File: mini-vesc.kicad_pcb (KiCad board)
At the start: 4 copper layers, 65 x 18 mm, 151 parts, among them P1 CONN_1, P10 CONN_01X06, P11 CONN_01X06, P2 CONN_1, P3 CONN_1, P4 CONN_1, P5 CONN_1, P6 CONN_1, P9 CONN_01X06, Q1 NTMFS5C604NLT1G, Q2 NTMFS5C604NLT1G, Q3 NTMFS5C604NLT1G, Q4 NTMFS5C604NLT1G, Q5 NTMFS5C604NLT1G, Q6 NTMFS5C604NLT1G, U1 LM5113, U10 MCP1700, U2 LM5113, U3 LM5113, U4 AD8418, U5 AD8418, U6 AD8418, U7 STM32F40X_LQFP64, U8 LMR16006, U9 MCP1700, X1 ABM3B-8.000MHZ

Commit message: Playing around with routing
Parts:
- removed C1, C2, C3: 470n, Capacitor_SMD:C_0603_1608Metric
- removed C10, C11, C17, C18, C6, C7, C77, C78, C8, C86, C87, C88, C89, C9, C90: 2u2, Capacitor_SMD:C_0603_1608Metric
- removed C12, C13, C25, C28, C32, C39, C4, C48, C5, C60, C61, C62, C63, C74, C75, C84, C85: 10u, Capacitor_SMD:C_1206_3216Metric
- removed C14, C15, C16: 4n7, Capacitor_SMD:C_0603_1608Metric
- removed C19, C20, C21, C22, C26, C27, C29, C76: 100n, Capacitor_SMD:C_0603_1608Metric
- removed C23: 220nF, Capacitor_SMD:C_0603_1608Metric
- removed C24: 2u2, Capacitor_SMD:C_1206_3216Metric
- removed C30, C31: 10pF, Capacitor_SMD:C_0603_1608Metric
- removed C33, C34, C35, C36, C37, C38, C40, C41, C42, C43, C44, C45, C46, C47, C49, C50, C51, C52, C53, C54, C55, C56, C57, C58, C59, C64, C65, C66, C67, C68, C69, C70, C71, C72, C73, C83: C, Capacitor_SMD:C_1206_3216Metric
- removed D1: D_Schottky, Diode_SMD:D_SOD-123
- removed D3, D4: LED, LED_SMD:LED_0603_1608Metric
- removed L1: Wurth Electronics 74438335220, mojaKniznica:WE-MAPI
- removed P1, P2, P3, P4, P5, P6: CONN_1, kicad_subory:prekov
- removed P10, P11, P9: CONN_01X06, kicad_subory:JST_ZH_1.5_6-Pin
- removed Q1, Q2, Q5, Q6: NTMFS5C604NLT1G, kicad_subory:DFN5
- removed R1, R2, R3: R0005, mojaKniznica:2512Rv2
- removed R10, R11, R6, R7, R8, R9: 3R9, Resistor_SMD:R_0603_1608Metric
- removed R12, R14, R4: 39k, Resistor_SMD:R_0603_1608Metric
- removed R13, R15, R17, R5: 2k2, Resistor_SMD:R_0603_1608Metric
- removed R16: 25k5, Resistor_SMD:R_0603_1608Metric
- removed R18, R19, R20, R30: 100R, Resistor_SMD:R_0603_1608Metric
- removed R21, R31, R34: 10k, Resistor_SMD:R_0603_1608Metric
- removed R28, R29: 220R, Resistor_SMD:R_0603_1608Metric
- removed R32: 10kNTC, Resistor_SMD:R_0603_1608Metric
- removed R33: 100k, Resistor_SMD:R_0603_1608Metric
- removed U1, U2, U3: LM5113, kicad_subory:WSON10_
- removed U10, U9: MCP1700, TO_SOT_Packages_SMD:SOT-23
- removed U4: AD8418, Package_SO:MSOP-8_3x3mm_P0.65mm
- removed U7: STM32F40X_LQFP64, Package_QFP:LQFP-64_10x10mm_P0.5mm
- removed U8: LMR16006, Package_TO_SOT_SMD:SOT-23-6
- removed X1: ABM3B-8.000MHZ, mojaKniznica:5x3.2KRISTALL
- added R23: 3.9Ω, Resistor_SMD:R_0402_1005Metric, F.Cu at (123.0, 68.8)
- added R24: 39kΩ, Resistor_SMD:R_0402_1005Metric, B.Cu at (119.7, 67.3)
- added R26: 500µΩ, Footprints:R_Shunt_Bourns_CSS2H-2512_6332Metric, B.Cu at (124.4, 64.0)
- C79: value 10u -> 2.2µF; footprint Capacitor_SMD:C_1206_3216Metric -> Capacitor_SMD:C_0402_1005Metric; moved to F.Cu
- C80: value 10u -> 470nF; footprint Capacitor_SMD:C_1206_3216Metric -> Capacitor_SMD:C_0402_1005Metric
- C81: value C -> 2.2µF; footprint Capacitor_SMD:C_1206_3216Metric -> Capacitor_SMD:C_0402_1005Metric
- C82: value 10u -> 4.7nF; footprint Capacitor_SMD:C_1206_3216Metric -> Capacitor_SMD:C_0402_1005Metric
- Q3: footprint kicad_subory:DFN5 -> Package_SO:ONSemi_SO-8FL_488AA; moved to F.Cu
- Q4: footprint kicad_subory:DFN5 -> Package_SO:ONSemi_SO-8FL_488AA
- R22: value 54k9 -> 3.9Ω; footprint Resistor_SMD:R_0603_1608Metric -> Resistor_SMD:R_0402_1005Metric
- R25: value 22R -> 2.2kΩ; footprint Resistor_SMD:R_0603_1608Metric -> Resistor_SMD:R_0402_1005Metric
- R27: value 22R -> 100Ω; footprint Resistor_SMD:R_0603_1608Metric -> Resistor_SMD:R_0402_1005Metric
- U5: value AD8418 -> LM5113-Q1; footprint Package_SO:MSOP-8_3x3mm_P0.65mm -> Footprints:WSON-10-1EP_4x4mm_P0.8mm_EP2.6x3mm_ThermalVias
- U6: value AD8418 -> AD8417; moved to B.Cu
- moved U5 52.8 mm to (119.9, 70.0)
- moved U6 52.7 mm to (124.4, 67.8), turned to 180 degrees
- moved Q4 48.8 mm to (121.4, 64.0)
- moved Q3 43.9 mm to (114.4, 64.0), turned to 180 degrees
- moved C81 30.1 mm to (120.7, 67.3), turned to -90 degrees
- moved C82 30.0 mm to (123.3, 70.5), turned to -90 degrees
- moved R25 29.4 mm to (118.7, 67.3), turned to -90 degrees
- moved R27 22.4 mm to (122.3, 70.5)
- moved C79 20.3 mm to (118.4, 67.3), turned to 0 degrees
- moved C80 18.7 mm to (117.3, 70.4), turned to -90 degrees
- moved R22 14.6 mm to (116.7, 70.4), turned to 90 degrees
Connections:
- C79 pad 1: VDD -> +5V
- C80 pad 1: VDD -> Net-(U5-HB)
- C80 pad 2: VSS -> /Half Bridge W/Output
- C81 pad 1: VDD -> VSS
- C81 pad 2: VSS -> VAA
- C82 pad 1: VDD -> VSS
- C82 pad 2: VSS -> I_{senseW}
- Q3 pad 1: Net-(Q3-G) -> /Half Bridge W/Output
- Q3 pad 2: SH2 -> /Half Bridge W/Output
- Q3 pad 3: VDD -> /Half Bridge W/Output
- Q4 pad 1: Net-(Q4-G) -> VSS
- Q4 pad 3: SH2 -> VSS
- R22 pad 1: +5V -> /Half Bridge W/HighGate
- R22 pad 2: Net-(U8-FB) -> Net-(U5-HOH)
- R25 pad 1: Net-(P10-Pin_4) -> VSS
- R25 pad 2: USB-DM -> V_{senseW}
- R27 pad 1: Net-(P10-Pin_5) -> Net-(U6-OUT)
- R27 pad 2: USB-DP -> I_{senseW}
- U5 pad 1: Net-(P2-Pad1) -> +5V
- U5 pad 2: VSS -> Net-(U5-HB)
- U5 pad 3: VSS -> Net-(U5-HOH)
- U5 pad 4: Net-(U5-Pad4) -> /Half Bridge W/HighGate
- U5 pad 5: I2 -> /Half Bridge W/Output
- U5 pad 6: VAA -> HI3
- U5 pad 7: VAA -> LI3
- U5 pad 8: SH2 -> VSS
- U6 pad 1: Net-(P3-Pad1) -> /W
- U6 pad 4: Net-(U6-Pad4) -> unconnected-(U6-NC-Pad4)
- U6 pad 5: I3 -> Net-(U6-OUT)
- U6 pad 8: SH3 -> /Half Bridge W/Output
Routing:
- net VSS: track 298.6 -> 8.32 mm, vias 57 -> 0
- net +5V: track 162.2 -> 1.11 mm, vias 6 -> 0
- net VAA: track 134.2 -> 3.44 mm, vias 6 -> 0
- net VDD: track 93.0 -> 0.00 mm, vias 30 -> 0
- net VCC: track 82.9 -> 0.00 mm, vias 6 -> 0
- net Net-(C77-Pad2): track 67.6 -> 0.00 mm
- net I1: track 60.9 -> 0.00 mm, vias 2 -> 0
- net I3: track 60.2 -> 0.00 mm, vias 2 -> 0
- net SENS_3: track 53.9 -> 0.00 mm, vias 2 -> 0
- net SENS_2: track 51.4 -> 0.00 mm, vias 2 -> 0
- net SENS_1: track 49.8 -> 0.00 mm, vias 2 -> 0
- net I2: track 48.2 -> 0.00 mm, vias 2 -> 0
- net ADC_EXT1: track 41.7 -> 0.00 mm, vias 3 -> 0
- net HI2: track 31.2 -> 0.00 mm, vias 2 -> 0
- net TX: track 29.4 -> 0.00 mm, vias 1 -> 0
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- added copper zone on B.Cu, net /Half Bridge W/Output
- added copper zone on F.Cu, net /Half Bridge W/Output
- removed copper zone on F.Cu, net +5V
- removed copper zone on F.Cu, net Net-(D1-K)
- removed copper zone on B.Cu, net Net-(U4-IN-)
- removed copper zone on F.Cu, net Net-(U4-IN-)
- removed copper zone on In1.Cu, net Net-(U4-IN-)
- removed copper zone on In2.Cu, net Net-(U4-IN-)
- removed copper zone on B.Cu, net Net-(U5-IN-)
- removed copper zone on F.Cu, net Net-(U5-IN-)
- removed copper zone on In1.Cu, net Net-(U5-IN-)
- removed copper zone on In2.Cu, net Net-(U5-IN-)
- removed copper zone on B.Cu, net Net-(U6-IN-)
- removed copper zone on F.Cu, net Net-(U6-IN-)
- removed copper zone on In1.Cu, net Net-(U6-IN-)
- removed copper zone on In2.Cu, net Net-(U6-IN-)
- removed copper zone on B.Cu, net SH1
- removed copper zone on F.Cu, net SH1
- removed copper zone on B.Cu, net SH2
- removed copper zone on F.Cu, net SH2
- removed copper zone on B.Cu, net SH3
- removed copper zone on F.Cu, net SH3
- removed copper zone on B.Cu, net VDD
- removed copper zone on F.Cu, net VDD
- removed copper zone on In1.Cu, net VDD
- removed copper zone on In2.Cu, net VDD
- removed copper zone on B.Cu, net VSS
- removed copper zone on F.Cu, net VSS
- removed copper zone on In1.Cu, net VSS
- removed copper zone on In2.Cu, net VSS
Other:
- board size 65 x 18 mm -> 65 x 40 mm
- board text removed: "+5V"
- board text removed: "A1"
- board text removed: "A2"
- board text removed: "DM"
- board text removed: "DP"
- board text removed: "GND"
- board text removed: "H1"
- board text removed: "H2"
- board text removed: "H3"
- board text removed: "PPM"
- board text removed: "RX"
- board text removed: "SWC"
- board text removed: "SWD"
- board text removed: "T"
- board text removed: "TX"

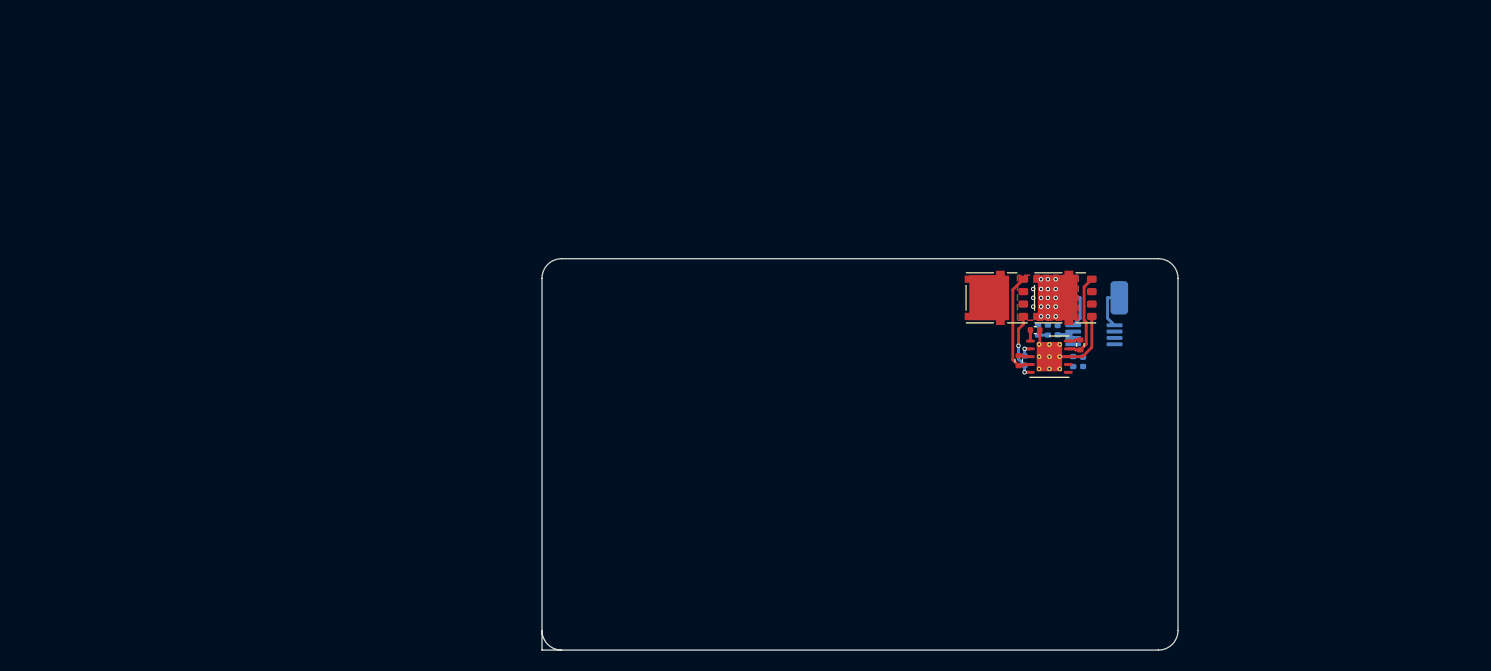
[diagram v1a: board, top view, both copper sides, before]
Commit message: Playing with routing some more, trying to determine board size
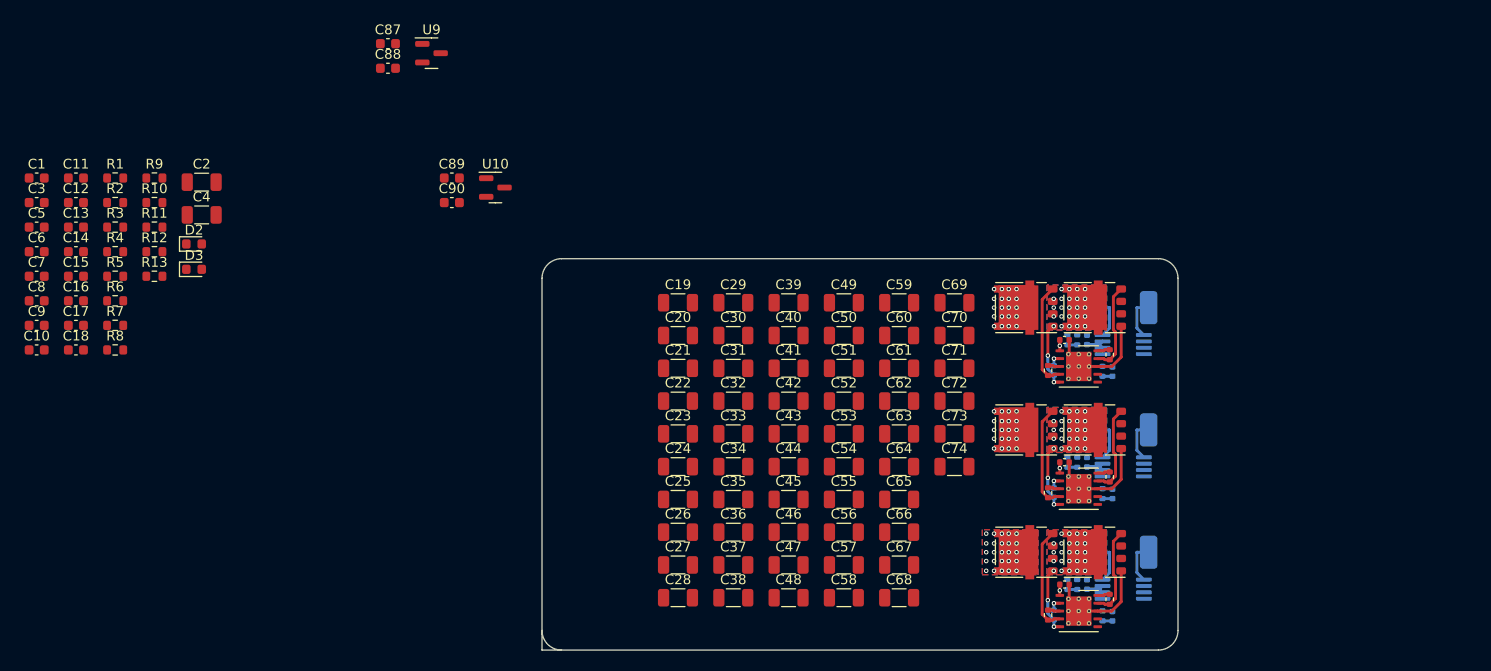
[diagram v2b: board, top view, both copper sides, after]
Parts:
- added C1: 220nF, Capacitor_SMD:C_0603_1608Metric, F.Cu at (16.4, 51.8)
- added C10: 2.2µF, Capacitor_SMD:C_0603_1608Metric, F.Cu at (16.4, 69.3)
- added C11: 2.2µF, Capacitor_SMD:C_0603_1608Metric, F.Cu at (20.4, 51.8)
- added C12: 10pF, Capacitor_SMD:C_0603_1608Metric, F.Cu at (20.4, 54.3)
- added C13: 2.2µF, Capacitor_SMD:C_0603_1608Metric, F.Cu at (20.4, 56.8)
- added C14: 2.2µF, Capacitor_SMD:C_0603_1608Metric, F.Cu at (20.4, 59.3)
- added C15: 100n, Capacitor_SMD:C_0603_1608Metric, F.Cu at (20.4, 61.8)
- added C16: 100nF, Capacitor_SMD:C_0603_1608Metric, F.Cu at (20.4, 64.3)
- added C17: 10pF, Capacitor_SMD:C_0603_1608Metric, F.Cu at (20.4, 66.8)
- added C18: 2.2µF, Capacitor_SMD:C_0603_1608Metric, F.Cu at (20.4, 69.3)
- added C19: 10u, Capacitor_SMD:C_1206_3216Metric, F.Cu at (81.9, 64.5)
- added C2: 2.2µF, Capacitor_SMD:C_1206_3216Metric, F.Cu at (33.2, 52.2)
- added C20: C, Capacitor_SMD:C_1206_3216Metric, F.Cu at (81.9, 67.8)
- added C21: C, Capacitor_SMD:C_1206_3216Metric, F.Cu at (81.9, 71.2)
- added C22: 10u, Capacitor_SMD:C_1206_3216Metric, F.Cu at (81.9, 74.5)
- added C23: C, Capacitor_SMD:C_1206_3216Metric, F.Cu at (81.9, 77.9)
- added C24: 10u, Capacitor_SMD:C_1206_3216Metric, F.Cu at (81.9, 81.2)
- added C25: C, Capacitor_SMD:C_1206_3216Metric, F.Cu at (81.9, 84.6)
- added C26: C, Capacitor_SMD:C_1206_3216Metric, F.Cu at (81.9, 88.0)
- added C27: C, Capacitor_SMD:C_1206_3216Metric, F.Cu at (81.9, 91.3)
- added C28: C, Capacitor_SMD:C_1206_3216Metric, F.Cu at (81.9, 94.7)
- added C29: 10u, Capacitor_SMD:C_1206_3216Metric, F.Cu at (87.5, 64.5)
- added C3: 100nF, Capacitor_SMD:C_0603_1608Metric, F.Cu at (16.4, 54.3)
- added C30: C, Capacitor_SMD:C_1206_3216Metric, F.Cu at (87.5, 67.8)
- added C31: 10u, Capacitor_SMD:C_1206_3216Metric, F.Cu at (87.5, 71.2)
- added C32: 10u, Capacitor_SMD:C_1206_3216Metric, F.Cu at (87.5, 74.5)
- added C33: C, Capacitor_SMD:C_1206_3216Metric, F.Cu at (87.5, 77.9)
- added C34: C, Capacitor_SMD:C_1206_3216Metric, F.Cu at (87.5, 81.2)
- added C35: C, Capacitor_SMD:C_1206_3216Metric, F.Cu at (87.5, 84.6)
- added C36: 10u, Capacitor_SMD:C_1206_3216Metric, F.Cu at (87.5, 88.0)
- added C37: C, Capacitor_SMD:C_1206_3216Metric, F.Cu at (87.5, 91.3)
- added C38: C, Capacitor_SMD:C_1206_3216Metric, F.Cu at (87.5, 94.7)
- added C39: 10u, Capacitor_SMD:C_1206_3216Metric, F.Cu at (93.2, 64.5)
- added C4: 10µF, Capacitor_SMD:C_1206_3216Metric, F.Cu at (33.2, 55.5)
- added C40: C, Capacitor_SMD:C_1206_3216Metric, F.Cu at (93.2, 67.8)
- added C41: C, Capacitor_SMD:C_1206_3216Metric, F.Cu at (93.2, 71.2)
- added C42: C, Capacitor_SMD:C_1206_3216Metric, F.Cu at (93.2, 74.5)
- added C43: C, Capacitor_SMD:C_1206_3216Metric, F.Cu at (93.2, 77.9)
- added C44: C, Capacitor_SMD:C_1206_3216Metric, F.Cu at (93.2, 81.2)
- added C45: C, Capacitor_SMD:C_1206_3216Metric, F.Cu at (93.2, 84.6)
- added C46: 10u, Capacitor_SMD:C_1206_3216Metric, F.Cu at (93.2, 88.0)
- added C47: C, Capacitor_SMD:C_1206_3216Metric, F.Cu at (93.2, 91.3)
- added C48: 10u, Capacitor_SMD:C_1206_3216Metric, F.Cu at (93.2, 94.7)
- added C49: C, Capacitor_SMD:C_1206_3216Metric, F.Cu at (98.8, 64.5)
- added C5: 100nF, Capacitor_SMD:C_0603_1608Metric, F.Cu at (16.4, 56.8)
- added C50: C, Capacitor_SMD:C_1206_3216Metric, F.Cu at (98.8, 67.8)
- added C51: C, Capacitor_SMD:C_1206_3216Metric, F.Cu at (98.8, 71.2)
- added C52: 10u, Capacitor_SMD:C_1206_3216Metric, F.Cu at (98.8, 74.5)
- added C53: 10u, Capacitor_SMD:C_1206_3216Metric, F.Cu at (98.8, 77.9)
- added C54: C, Capacitor_SMD:C_1206_3216Metric, F.Cu at (98.8, 81.2)
- added C55: C, Capacitor_SMD:C_1206_3216Metric, F.Cu at (98.8, 84.6)
- added C56: C, Capacitor_SMD:C_1206_3216Metric, F.Cu at (98.8, 88.0)
- added C57: C, Capacitor_SMD:C_1206_3216Metric, F.Cu at (98.8, 91.3)
- added C58: C, Capacitor_SMD:C_1206_3216Metric, F.Cu at (98.8, 94.7)
- added C59: 10u, Capacitor_SMD:C_1206_3216Metric, F.Cu at (104.5, 64.5)
- added C6: 100nF, Capacitor_SMD:C_0603_1608Metric, F.Cu at (16.4, 59.3)
- added C60: 10u, Capacitor_SMD:C_1206_3216Metric, F.Cu at (104.5, 67.8)
- added C61: C, Capacitor_SMD:C_1206_3216Metric, F.Cu at (104.5, 71.2)
- added C62: C, Capacitor_SMD:C_1206_3216Metric, F.Cu at (104.5, 74.5)
- added C63: 10u, Capacitor_SMD:C_1206_3216Metric, F.Cu at (104.5, 77.9)
- added C64: C, Capacitor_SMD:C_1206_3216Metric, F.Cu at (104.5, 81.2)
- added C65: C, Capacitor_SMD:C_1206_3216Metric, F.Cu at (104.5, 84.6)
- added C66: 10u, Capacitor_SMD:C_1206_3216Metric, F.Cu at (104.5, 88.0)
- added C67: 10u, Capacitor_SMD:C_1206_3216Metric, F.Cu at (104.5, 91.3)
- added C68: C, Capacitor_SMD:C_1206_3216Metric, F.Cu at (104.5, 94.7)
- added C69: C, Capacitor_SMD:C_1206_3216Metric, F.Cu at (110.2, 64.5)
- added C7: 100nF, Capacitor_SMD:C_0603_1608Metric, F.Cu at (16.4, 61.8)
- added C70: 10u, Capacitor_SMD:C_1206_3216Metric, F.Cu at (110.2, 67.8)
- added C71: C, Capacitor_SMD:C_1206_3216Metric, F.Cu at (110.2, 71.2)
- added C72: C, Capacitor_SMD:C_1206_3216Metric, F.Cu at (110.2, 74.5)
- added C73: 10u, Capacitor_SMD:C_1206_3216Metric, F.Cu at (110.2, 77.9)
- added C74: C, Capacitor_SMD:C_1206_3216Metric, F.Cu at (110.2, 81.2)
- added C75: 2.2µF, Capacitor_SMD:C_0402_1005Metric, F.Cu at (121.4, 68.3)
- added C76: 470nF, Capacitor_SMD:C_0402_1005Metric, B.Cu at (120.3, 71.4)
- added C77: 2.2µF, Capacitor_SMD:C_0402_1005Metric, B.Cu at (123.7, 68.3)
- added C78: 4.7nF, Capacitor_SMD:C_0402_1005Metric, B.Cu at (126.3, 71.5)
- added C8: 100nF, Capacitor_SMD:C_0603_1608Metric, F.Cu at (16.4, 64.3)
- added C83: 2.2µF, Capacitor_SMD:C_0402_1005Metric, F.Cu at (121.4, 80.8)
- added C84: 470nF, Capacitor_SMD:C_0402_1005Metric, B.Cu at (120.3, 83.9)
- added C85: 2.2µF, Capacitor_SMD:C_0402_1005Metric, B.Cu at (123.7, 80.8)
- added C86: 4.7nF, Capacitor_SMD:C_0402_1005Metric, B.Cu at (126.3, 84.0)
- added C87: 2.2µF, Capacitor_SMD:C_0603_1608Metric, F.Cu at (52.3, 38.0)
- added C88: 2.2µF, Capacitor_SMD:C_0603_1608Metric, F.Cu at (52.3, 40.5)
- added C89: 2.2µF, Capacitor_SMD:C_0603_1608Metric, F.Cu at (58.8, 51.8)
- added C9: 100nF, Capacitor_SMD:C_0603_1608Metric, F.Cu at (16.4, 66.8)
- added C90: 2.2µF, Capacitor_SMD:C_0603_1608Metric, F.Cu at (58.8, 54.3)
- added D2: LED, LED_SMD:LED_0603_1608Metric, F.Cu at (32.4, 58.5)
- added D3: LED, LED_SMD:LED_0603_1608Metric, F.Cu at (32.4, 61.1)
- added Q1: NTMFS5C604NLT1G, Package_SO:ONSemi_SO-8FL_488AA, F.Cu at (117.4, 65.0)
- added Q2: NTMFS5C604NLT1G, Package_SO:ONSemi_SO-8FL_488AA, F.Cu at (124.4, 65.0)
- added Q5: NTMFS5C604NLT1G, Package_SO:ONSemi_SO-8FL_488AA, F.Cu at (117.4, 77.5)
- added Q6: NTMFS5C604NLT1G, Package_SO:ONSemi_SO-8FL_488AA, F.Cu at (124.4, 77.5)
- added R1: 10kΩ, Resistor_SMD:R_0603_1608Metric, F.Cu at (24.4, 51.8)
- added R10: 10kΩ, Resistor_SMD:R_0603_1608Metric, F.Cu at (28.4, 54.3)
- added R11: 10kΩ, Resistor_SMD:R_0603_1608Metric, F.Cu at (28.4, 56.8)
- added R12: 22Ω, Resistor_SMD:R_0603_1608Metric, F.Cu at (28.4, 59.3)
- added R13: 22Ω, Resistor_SMD:R_0603_1608Metric, F.Cu at (28.4, 61.8)
- added R15: 3.9Ω, Resistor_SMD:R_0402_1005Metric, F.Cu at (119.7, 71.4)
- added R16: 3.9Ω, Resistor_SMD:R_0402_1005Metric, F.Cu at (126.0, 69.8)
- added R17: 39kΩ, Resistor_SMD:R_0402_1005Metric, B.Cu at (122.7, 68.3)
- added R18: 2.2kΩ, Resistor_SMD:R_0402_1005Metric, B.Cu at (121.7, 68.3)
- added R19: 500µΩ, Footprints:R_Shunt_Bourns_CSS2H-2512_6332Metric, B.Cu at (127.4, 65.0)
- added R2: 54.9kΩ, Resistor_SMD:R_0603_1608Metric, F.Cu at (24.4, 54.3)
- added R20: 100Ω, Resistor_SMD:R_0402_1005Metric, B.Cu at (125.3, 71.5)
- added R29: 3.9Ω, Resistor_SMD:R_0402_1005Metric, F.Cu at (119.7, 83.9)
- added R3: 100kΩ, Resistor_SMD:R_0603_1608Metric, F.Cu at (24.4, 56.8)
- added R30: 3.9Ω, Resistor_SMD:R_0402_1005Metric, F.Cu at (126.0, 82.3)
- added R31: 39kΩ, Resistor_SMD:R_0402_1005Metric, B.Cu at (122.7, 80.8)
- added R32: 2.2kΩ, Resistor_SMD:R_0402_1005Metric, B.Cu at (121.7, 80.8)
- added R33: 500µΩ, Footprints:R_Shunt_Bourns_CSS2H-2512_6332Metric, B.Cu at (127.4, 77.5)
- added R34: 100Ω, Resistor_SMD:R_0402_1005Metric, B.Cu at (125.3, 84.0)
- added R4: 100Ω, Resistor_SMD:R_0603_1608Metric, F.Cu at (24.4, 59.3)
- added R5: 39kΩ, Resistor_SMD:R_0603_1608Metric, F.Cu at (24.4, 61.8)
- added R6: 2.2kΩ, Resistor_SMD:R_0603_1608Metric, F.Cu at (24.4, 64.3)
- added R7: 220Ω, Resistor_SMD:R_0603_1608Metric, F.Cu at (24.4, 66.8)
- added R8: 220Ω, Resistor_SMD:R_0603_1608Metric, F.Cu at (24.4, 69.3)
- added R9: 10kΩ, Resistor_SMD:R_0603_1608Metric, F.Cu at (28.4, 51.8)
- added U10: MCP1700x-330xxTT, Package_TO_SOT_SMD:SOT-23, F.Cu at (63.2, 52.7)
- added U3: LM5113-Q1, Footprints:WSON-10-1EP_4x4mm_P0.8mm_EP2.6x3mm_ThermalVias, F.Cu at (122.9, 71.0)
- added U4: AD8417, Package_SO:MSOP-8_3x3mm_P0.65mm, B.Cu at (127.4, 68.8)
- added U7: LM5113-Q1, Footprints:WSON-10-1EP_4x4mm_P0.8mm_EP2.6x3mm_ThermalVias, F.Cu at (122.9, 83.5)
- added U8: AD8417, Package_SO:MSOP-8_3x3mm_P0.65mm, B.Cu at (127.4, 81.3)
- added U9: MCP1700x-330xxTT, Package_TO_SOT_SMD:SOT-23, F.Cu at (56.7, 39.0)
- moved C79 26.2 mm to (121.4, 93.3)
- moved C80 26.2 mm to (120.3, 96.4)
- moved C81 26.2 mm to (123.7, 93.3)
- moved C82 26.2 mm to (126.3, 96.5)
- moved Q3 26.2 mm to (117.4, 90.0)
- moved Q4 26.2 mm to (124.4, 90.0)
- moved R22 26.2 mm to (119.7, 96.4)
- moved R23 26.2 mm to (126.0, 94.8)
- moved R24 26.2 mm to (122.7, 93.3)
- moved R25 26.2 mm to (121.7, 93.3)
- moved R26 26.2 mm to (127.4, 90.0)
- moved R27 26.2 mm to (125.3, 96.5)
- moved U5 26.2 mm to (122.9, 96.0)
- moved U6 26.2 mm to (127.4, 93.8)
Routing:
- net VSS: track 8.32 -> 25.0 mm
- net /Half Bridge V/Output: track 0.00 -> 11.1 mm, vias 0 -> 26
- net /Half Bridge U/Output: track 0.00 -> 11.1 mm, vias 0 -> 26
- net /Half Bridge V/HighGate: track 0.00 -> 10.8 mm
- net /Half Bridge U/HighGate: track 0.00 -> 10.8 mm
- net /Half Bridge V/LowGate: track 0.00 -> 9.16 mm
- net /Half Bridge U/LowGate: track 0.00 -> 9.16 mm
- net VAA: track 3.44 -> 10.3 mm
- net /V: track 0.00 -> 4.30 mm
- net /U: track 0.00 -> 4.30 mm
- net +5V: track 1.11 -> 3.34 mm, vias 0 -> 3
- net Net-(U7-HB): track 0.00 -> 1.32 mm, vias 0 -> 1
- net Net-(U3-HB): track 0.00 -> 1.32 mm, vias 0 -> 1
- net Net-(U7-LOH): track 0.00 -> 1.27 mm
- net Net-(U3-LOH): track 0.00 -> 1.27 mm
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- added copper zone on B.Cu, net /Half Bridge U/Output
- added copper zone on F.Cu, net /Half Bridge U/Output
- added copper zone on B.Cu, net /Half Bridge V/Output
- added copper zone on F.Cu, net /Half Bridge V/Output
- added copper zone on B.Cu, net VDD
- added copper zone on F.Cu, net VDD

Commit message: More work
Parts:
- C40, C41, C42, C43, C44, C45, C46, C47, C48, C49, C50, C51, C52, C53, C54, C55, C56, C57, C58, C59, C60, C61, C62, C63, C64, C65, C66, C67, C68, C69, C70, C71, C72, C73, C74, Q2, Q4, Q6: moved to B.Cu
- C77, C78, C81, C82, C85, C86, R17, R18, R20, R24, R25, R27, R31, R32, R34, U4, U6, U8: moved to F.Cu
- moved C28 56.4 mm to (129.5, 64.4)
- moved C27 55.8 mm to (129.5, 62.2)
- moved C26 55.2 mm to (129.5, 60.0)
- moved C38 52.1 mm to (134.0, 71.0), turned to 180 degrees
- moved C68 51.8 mm to (143.0, 60.0), turned to 180 degrees
- moved C37 51.6 mm to (134.0, 68.8), turned to 180 degrees
- moved C36 51.1 mm to (134.0, 66.6), turned to 180 degrees
- moved C35 50.6 mm to (134.0, 64.4), turned to 180 degrees
- moved C34 50.2 mm to (134.0, 62.2), turned to 180 degrees
- moved C33 49.8 mm to (134.0, 60.0), turned to 180 degrees
- moved C48 48.7 mm to (129.5, 62.2)
- moved C47 47.9 mm to (129.5, 60.0)
- moved C25 44.6 mm to (125.0, 73.2), turned to 180 degrees
- moved C24 44.3 mm to (125.0, 71.0), turned to 180 degrees
- moved C23 44.0 mm to (125.0, 68.8), turned to 180 degrees
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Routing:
- net VSS: track 25.0 -> 0.00 mm
- net /Half Bridge W/Output: track 11.1 -> 0.00 mm, vias 26 -> 0
- net /Half Bridge V/Output: track 11.1 -> 0.00 mm, vias 26 -> 0
- net /Half Bridge U/Output: track 11.1 -> 0.00 mm, vias 26 -> 0
- net /Half Bridge W/HighGate: track 10.8 -> 0.00 mm
- net /Half Bridge V/HighGate: track 10.8 -> 0.00 mm
- net /Half Bridge U/HighGate: track 10.8 -> 0.00 mm
- net VAA: track 10.3 -> 0.00 mm
- net /Half Bridge W/LowGate: track 9.16 -> 0.00 mm
- net /Half Bridge V/LowGate: track 9.16 -> 0.00 mm
- net /Half Bridge U/LowGate: track 9.16 -> 0.00 mm
- net /W: track 4.30 -> 0.00 mm
- net /V: track 4.30 -> 0.00 mm
- net /U: track 4.30 -> 0.00 mm
- net +5V: track 3.34 -> 0.00 mm, vias 3 -> 0
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- removed copper zone on B.Cu, net /Half Bridge U/Output
- removed copper zone on F.Cu, net /Half Bridge U/Output
- removed copper zone on B.Cu, net /Half Bridge V/Output
- removed copper zone on F.Cu, net /Half Bridge V/Output
- removed copper zone on B.Cu, net /Half Bridge W/Output
- removed copper zone on F.Cu, net /Half Bridge W/Output
- removed copper zone on B.Cu, net VDD
- removed copper zone on F.Cu, net VDD

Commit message: Did something I think?
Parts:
- added U5: LMG1205, Footprints:Texas_YFX0012_DSBGA-12_1.76x1.91mm_Layout3x4_P0.4mm, F.Cu at (100.4, 54.0)
- added U7: LMG1205, Footprints:Texas_YFX0012_DSBGA-12_1.76x1.91mm_Layout3x4_P0.4mm, F.Cu at (100.4, 61.0)
- C15: value 100n -> 100nF
- C19, C22, C24, C29, C31, C32, C36, C39, C46, C48, C52, C53, C59, C60, C63, C66, C67, C70, C73: value 10u -> 2.2µF
- C20, C21, C23, C25, C26, C27, C28, C30, C33, C34, C35, C37, C38, C40, C41, C42, C43, C44, C45, C47, C49, C50, C51, C54, C55, C56, C57, C58, C61, C62, C64, C65, C68, C69, C71, C72, C74: value C -> 2.2µF
- U3: value LM5113-Q1 -> LMG1205; footprint Footprints:WSON-10-1EP_4x4mm_P0.8mm_EP2.6x3mm_ThermalVias -> Footprints:Texas_YFX0012_DSBGA-12_1.76x1.91mm_Layout3x4_P0.4mm
- moved R16 9.74 mm to (144.5, 52.0)
- moved U3 8.93 mm to (143.3, 51.4), turned to 180 degrees
- moved R15 7.96 mm to (144.5, 50.0), turned to 180 degrees
- moved C76 7.74 mm to (142.5, 50.0)
- moved C75 4.56 mm to (143.0, 54.0), turned to 0 degrees
- moved R29 0.16 mm to (140.5, 63.5)
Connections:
- C76 pad 2: /Half Bridge U/Output -> HS
- C80 pad 2: /Half Bridge W/Output -> HS
- C84 pad 2: /Half Bridge V/Output -> HS
- Q1 pad 1: /Half Bridge U/Output -> HS
- Q1 pad 2: /Half Bridge U/Output -> HS
- Q1 pad 3: /Half Bridge U/Output -> HS
- Q2 pad 5: /Half Bridge U/Output -> HS
- Q3 pad 1: /Half Bridge W/Output -> HS
- Q3 pad 2: /Half Bridge W/Output -> HS
- Q3 pad 3: /Half Bridge W/Output -> HS
- Q4 pad 5: /Half Bridge W/Output -> HS
- Q5 pad 1: /Half Bridge V/Output -> HS
- Q5 pad 2: /Half Bridge V/Output -> HS
- Q5 pad 3: /Half Bridge V/Output -> HS
- Q6 pad 5: /Half Bridge V/Output -> HS
- R17 pad 2: /Half Bridge U/Output -> HS
- R19 pad 2: /Half Bridge U/Output -> HS
- R24 pad 2: /Half Bridge W/Output -> HS
- R26 pad 2: /Half Bridge W/Output -> HS
- R31 pad 2: /Half Bridge V/Output -> HS
- R33 pad 2: /Half Bridge V/Output -> HS
- U4 pad 8: /Half Bridge U/Output -> HS
- U6 pad 8: /Half Bridge W/Output -> HS
- U8 pad 8: /Half Bridge V/Output -> HS
